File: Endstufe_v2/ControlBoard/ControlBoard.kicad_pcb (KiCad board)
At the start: 4 copper layers, 100 x 85 mm, 229 parts, among them J1 B4B-XH-2_(LF)(SN), J10 DNP, J11 DNP, J12 DNP, J13 DNP, J14 DAC all outputs, J15 B4B-XH-2_(LF)(SN), J16 B6B-XH-2(LF)(SN), J2 B4B-XH-2_(LF)(SN), J3 B4B-XH-2_(LF)(SN), J4 DNP, J5 B6B-XH-2(LF)(SN), J6 Conn_01x02_Pin, J7 DNP, J8 DNP, J9 DNP, SW1 TS-1187A-B-A-B, SW2 TS-1187A-B-A-B, U1 NVTFWS014P04M8LTAG, U10 ADAU1962AWBSTZ, U2 1SMA5927A, U3 TPS62933, U4 TYPE-C 16PFS 2JCB1.2-H6.5 IPX8, U5 W25Q128JVS, U6 RP2040, U7 W25Q128JVS, U8 ADAU1467WBCPZ300, U9 ZPLR135_T8, Y1 12Mhz, Y2 24.576Mhz, Y3 24.576Mhz

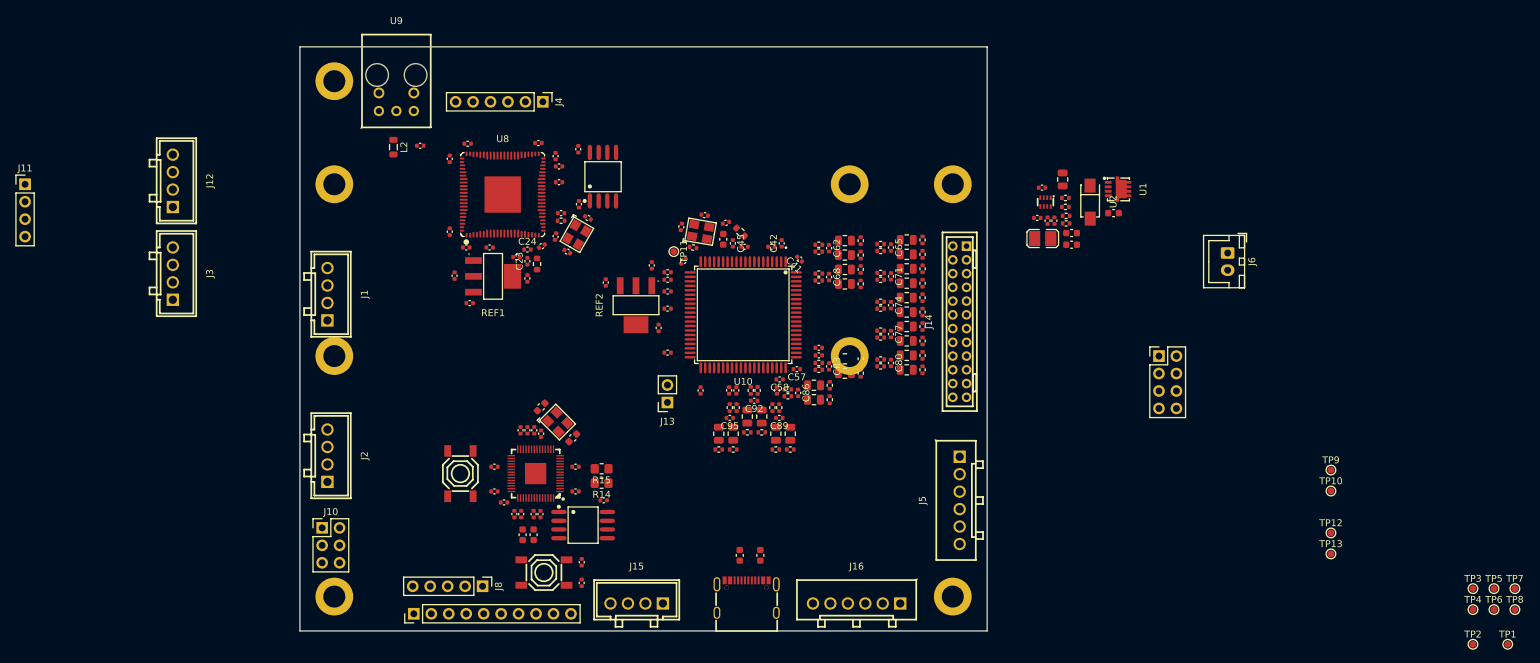
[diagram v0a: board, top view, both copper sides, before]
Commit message: Finish layout of control and input board for now
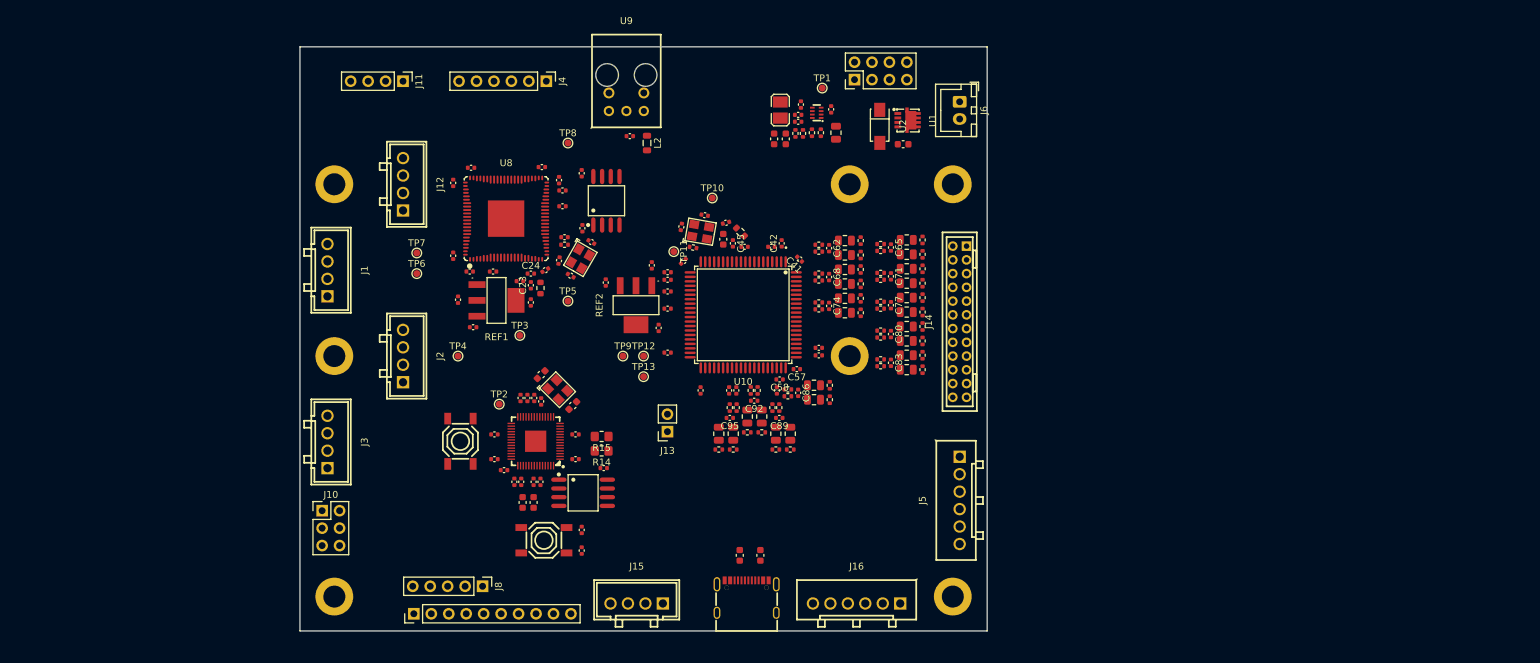
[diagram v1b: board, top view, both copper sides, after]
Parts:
- removed H6: MountingHole_Pad, Endstufe:MountingHole_3.2mm_M3_ISO14580_Pad
- moved TP7 167.1 mm to (87.0, 100.0)
- moved TP6 164.2 mm to (87.0, 103.0)
- moved TP8 153.6 mm to (109.0, 84.0)
- moved TP4 152.2 mm to (93.0, 115.0)
- moved TP2 145.9 mm to (99.0, 122.0)
- moved TP3 143.5 mm to (102.0, 112.0)
- moved TP5 141.1 mm to (109.0, 107.0)
- moved TP1 128.5 mm to (146.0, 76.0)
- moved TP9 104.4 mm to (117.0, 115.0)
- moved TP13 103.3 mm to (120.0, 118.0)
- moved TP12 103.3 mm to (120.0, 115.0)
- moved TP10 99.6 mm to (130.0, 92.0)
- moved J7 59.8 mm to (150.7, 74.8), turned to 90 degrees
- moved J11 57.0 mm to (85.0, 75.0), turned to -90 degrees
- moved C6 45.9 mm to (139.0, 83.4), turned to -90 degrees
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
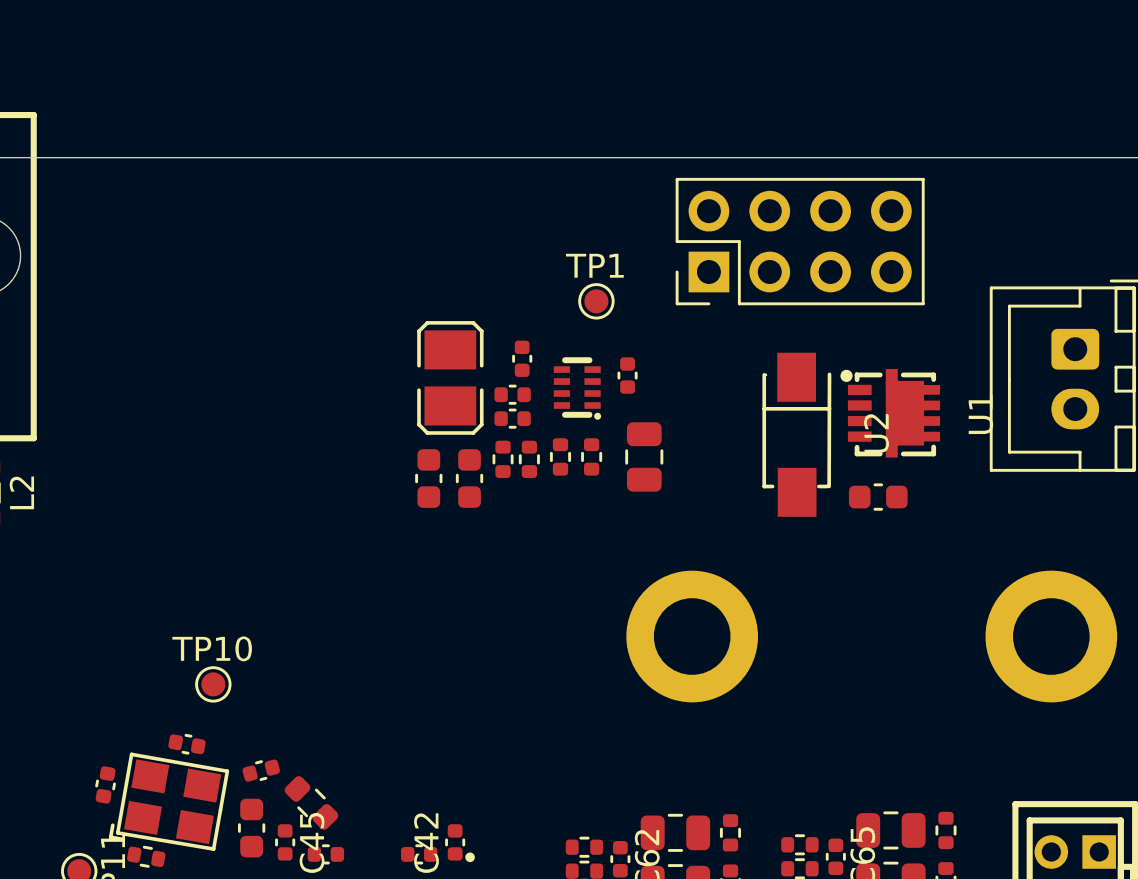
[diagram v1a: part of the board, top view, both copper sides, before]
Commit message: Add forgotten 3V3 outputs to control board
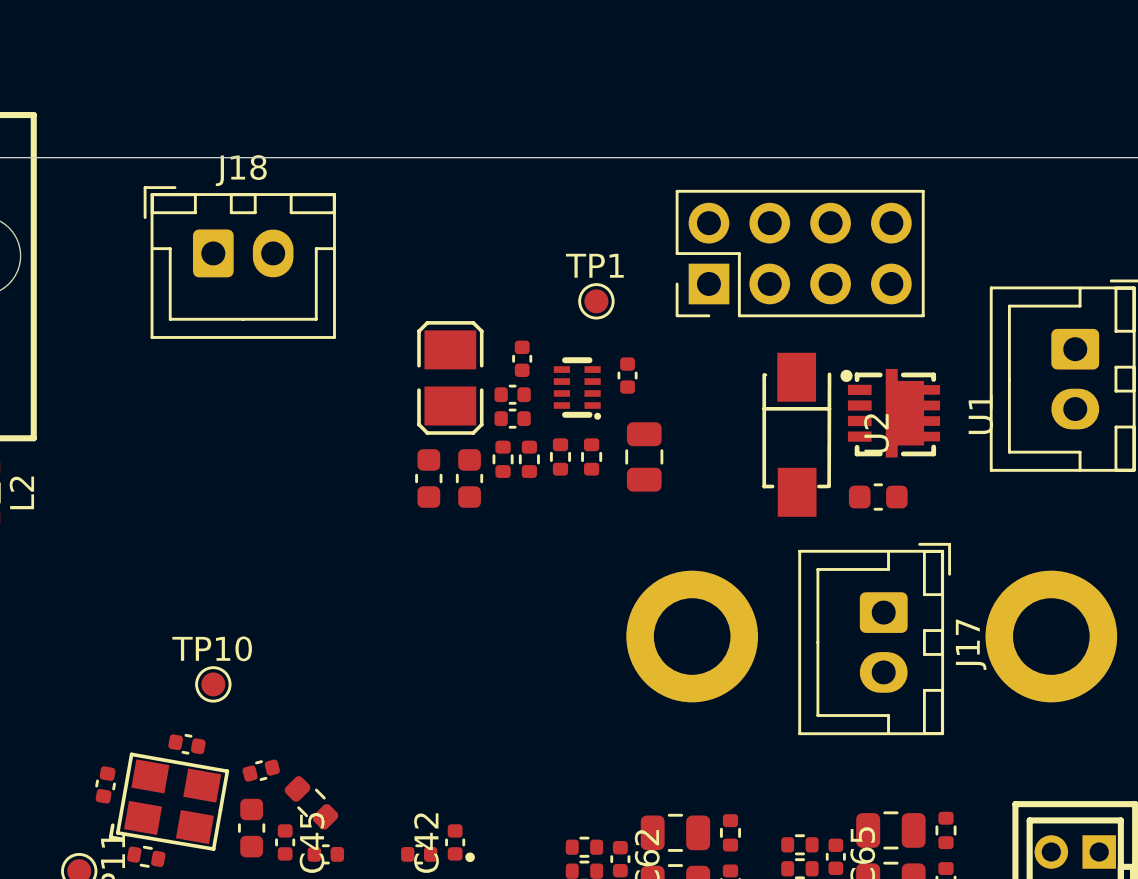
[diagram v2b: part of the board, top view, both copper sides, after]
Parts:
- added J17: Conn_01x02_Pin, Connector_JST:JST_XH_B2B-XH-A_1x02_P2.50mm_Vertical, F.Cu at (158.0, 89.0)
- added J18: Conn_01x02_Pin, Connector_JST:JST_XH_B2B-XH-A_1x02_P2.50mm_Vertical, F.Cu at (130.0, 74.0)
- moved J7 0.50 mm to (150.7, 75.3)

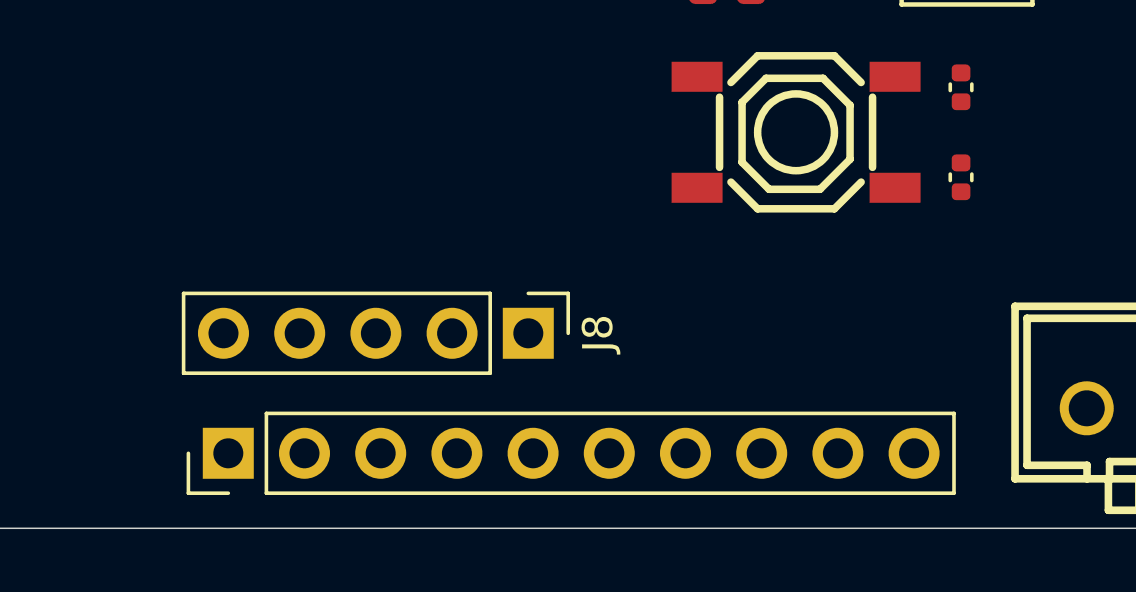
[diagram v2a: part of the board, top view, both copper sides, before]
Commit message: Add additional I2C headers
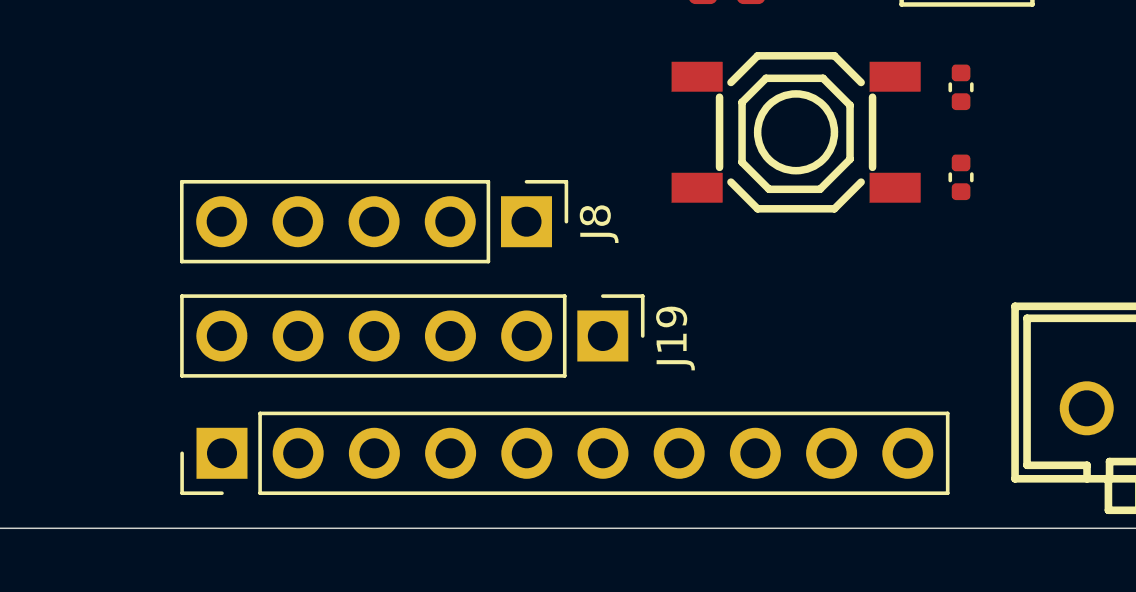
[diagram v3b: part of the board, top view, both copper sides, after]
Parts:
- added J19: Conn_01x06_Pin, Connector_PinHeader_2.54mm:PinHeader_1x06_P2.54mm_Vertical, F.Cu at (99.1, 148.6)
- moved J8 3.72 mm to (96.5, 144.8)
- moved J9 0.21 mm to (86.4, 152.5)
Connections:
- J9 pad 10: unconnected-(J9-Pin_10-Pad10) -> Net-(J9-Pin_10)
- J9 pad 9: unconnected-(J9-Pin_9-Pad9) -> Net-(J9-Pin_9)
- U6 pad 29: unconnected-(U6-GPIO18-Pad29) -> Net-(J9-Pin_10)
- U6 pad 30: unconnected-(U6-GPIO19-Pad30) -> Net-(J9-Pin_9)

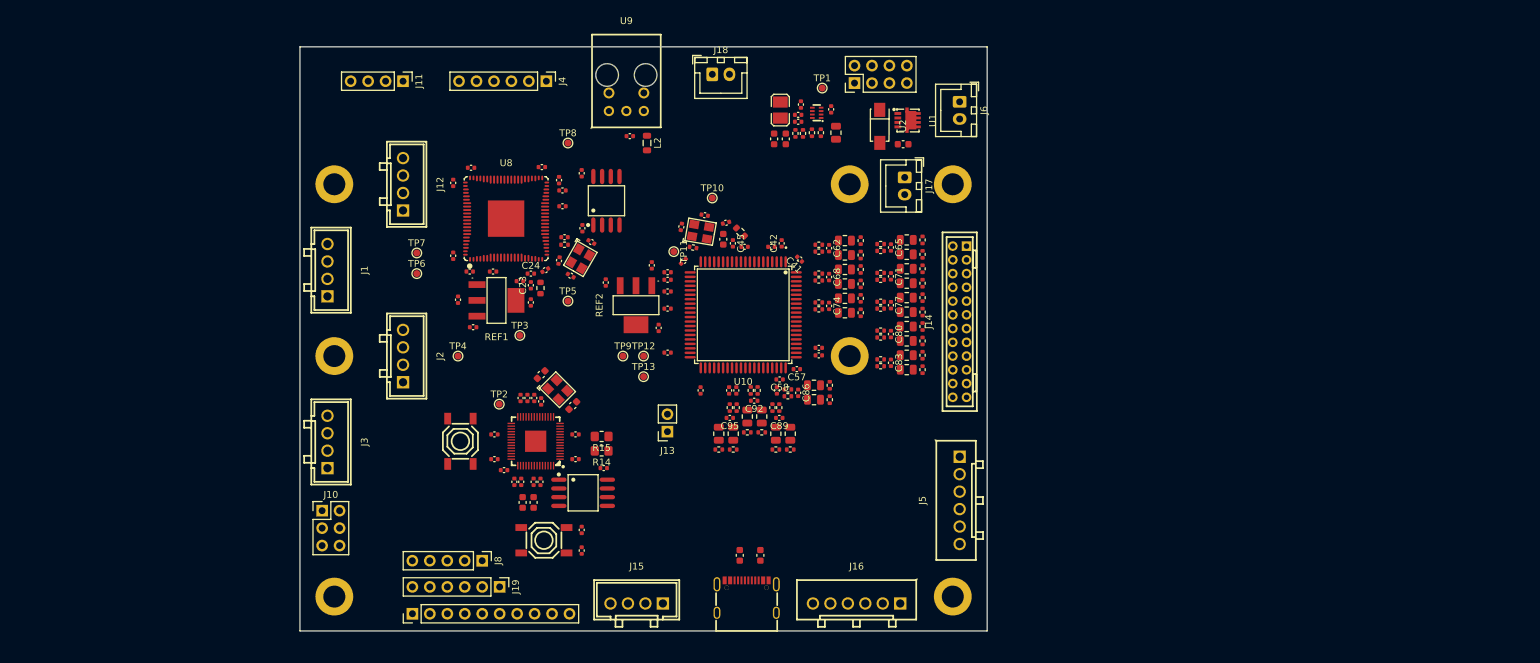
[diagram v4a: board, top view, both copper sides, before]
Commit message: Route control board
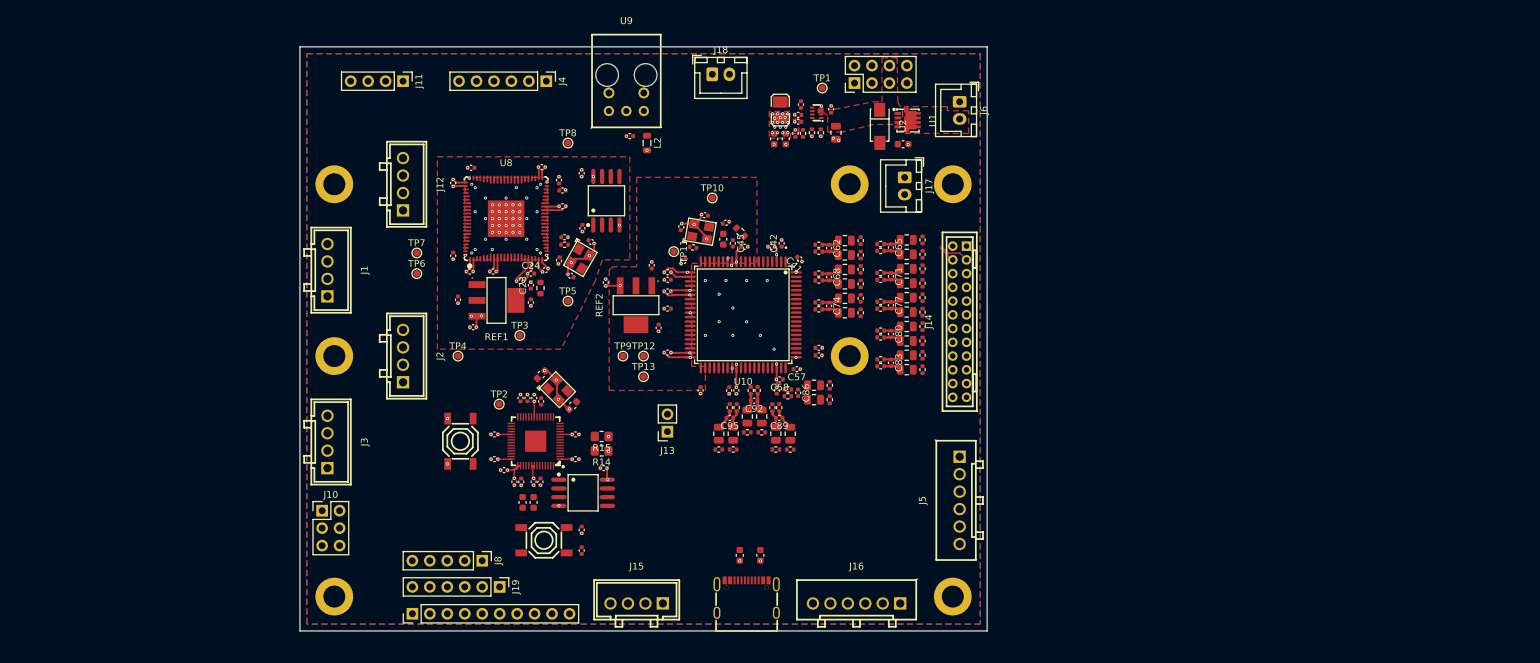
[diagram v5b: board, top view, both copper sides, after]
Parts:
- turned R56 to -90 degrees
- turned R57 to 90 degrees
- turned R72 to 180 degrees
- turned R73 to 0 degrees
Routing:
- net +3V3: track 0.00 -> 56.1 mm, vias 0 -> 70
- net GND: track 0.00 -> 50.4 mm, vias 0 -> 144
- net /ADAU1962A/DAC_Filter1/OUTPUTxN: track 0.00 -> 4.59 mm
- net Net-(C89-Pad1): track 0.00 -> 3.00 mm
- net Net-(C95-Pad2): track 0.00 -> 3.00 mm
- net Net-(C77-Pad1): track 0.00 -> 2.61 mm
- net Net-(C65-Pad1): track 0.00 -> 2.61 mm
- net Net-(C71-Pad1): track 0.00 -> 2.61 mm
- net Net-(C83-Pad1): track 0.00 -> 2.59 mm
- net Net-(C74-Pad1): track 0.00 -> 2.59 mm
- net Net-(C80-Pad1): track 0.00 -> 2.59 mm
- net Net-(C68-Pad1): track 0.00 -> 2.59 mm
- net Net-(C62-Pad1): track 0.00 -> 2.59 mm
- net Net-(C92-Pad1): track 0.00 -> 2.59 mm
- net /ADAU1962A/DAC_Filter1/OUTPUTxP: track 0.00 -> 2.59 mm
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- added copper zone on F.Cu, net +1V2
- added copper zone on F.Cu, net +24V
- added copper zone on F.Cu, net +2V5
- added copper zone on B.Cu, net +3V3
- added copper zone on F.Cu, net +3V3
- added copper zone on F.Cu, net GND
- added copper zone on In2.Cu, net GND
- added copper zone on F.Cu, net Net-(J6-Pin_2)
